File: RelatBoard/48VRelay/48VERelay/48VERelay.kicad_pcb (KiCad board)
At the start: 4 copper layers, 120 x 90 mm, 103 parts, among them J1 12, J10 Screw_Terminal_01x03, J11 Screw_Terminal_01x03, J12 Screw_Terminal_01x03, J13 Screw_Terminal_01x03, J14 Screw_Terminal_01x03, J2 RJ45_Hanrun_HR911105A_Horizon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, J4 TC2050, K10 G2RL-1-E, K11 G2RL-1-E, K12 G2RL-1-E, K13 G2RL-1-E, K14 G2RL-1-E, U1 ESP32-WROOM-32UE, U10 TLV1117LV33DCYR, U2 ULN2803A, U3 W5500, U4 3A 32V, U5 TPS630701RNMR, U7 TVS1800DRVR, U9 TLV1117LV33DCYR, Y2 ABM3C-25.000MHZ-D4Y-T

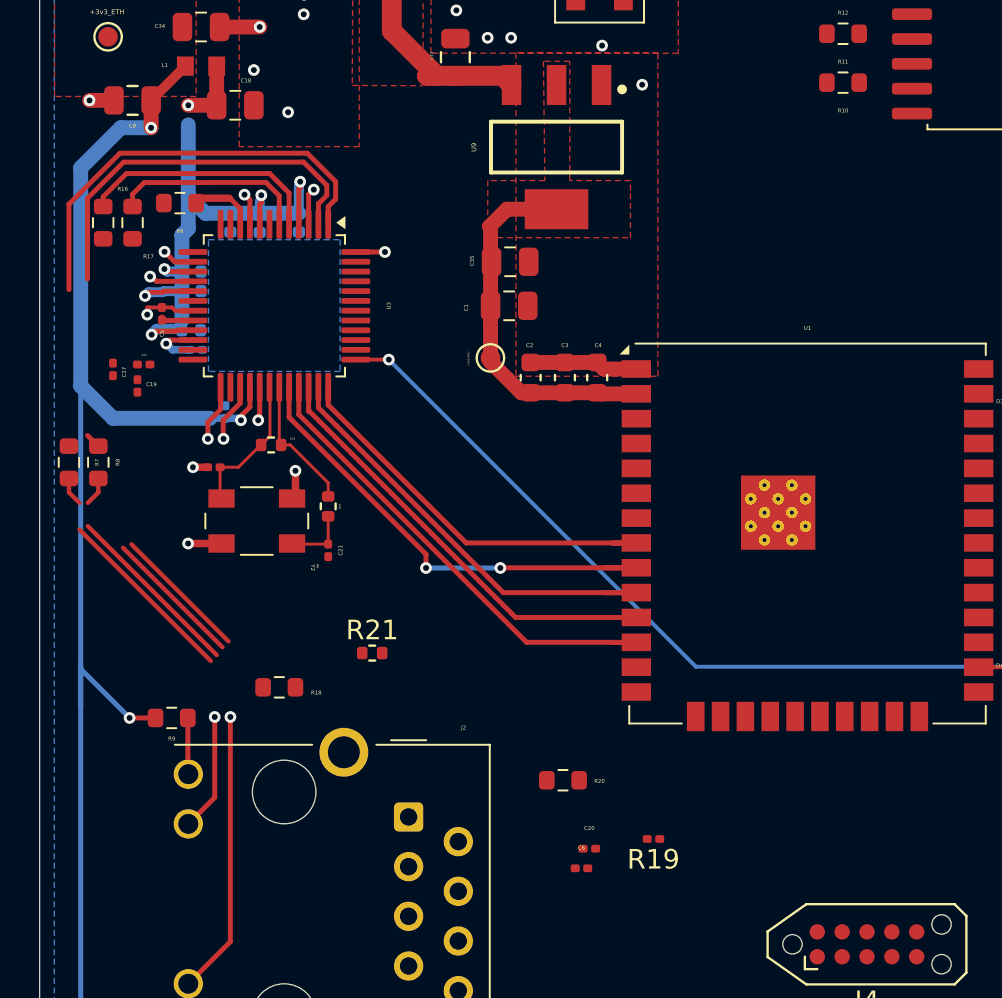
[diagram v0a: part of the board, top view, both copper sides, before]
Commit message: update tx/rx eth routing
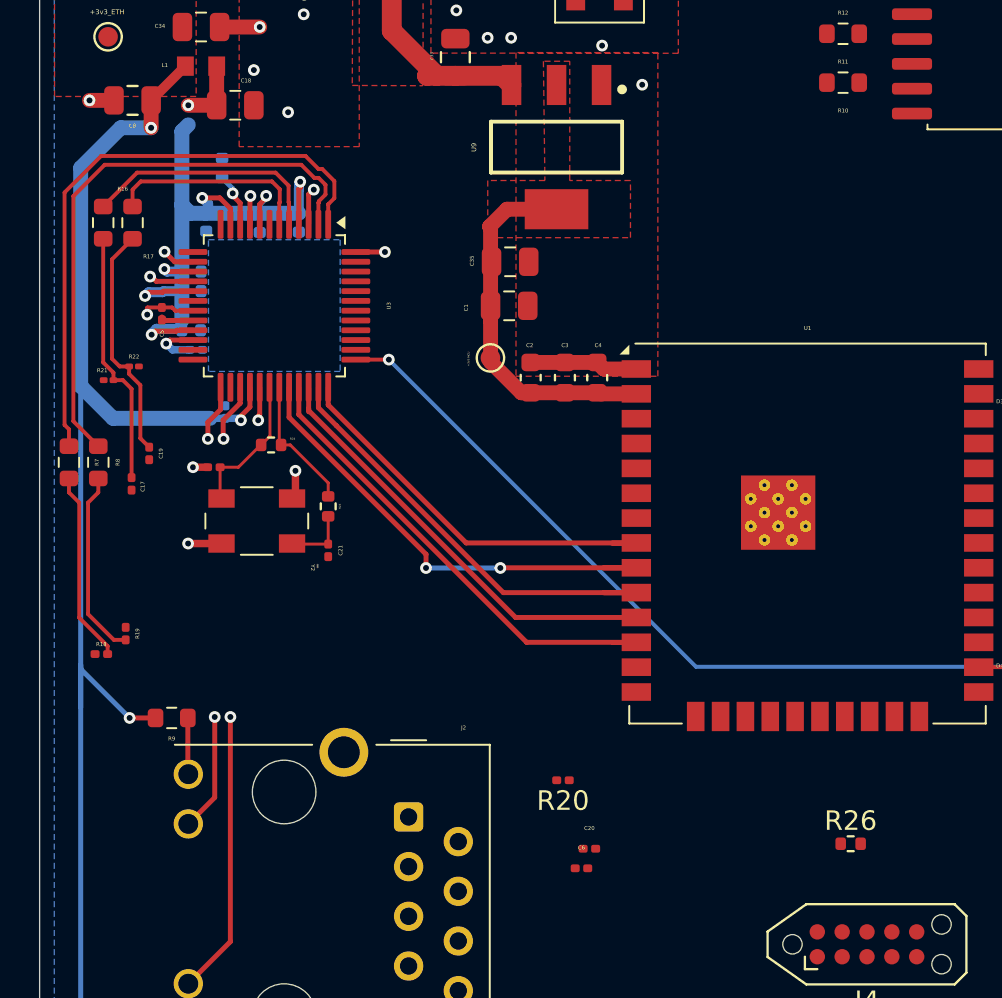
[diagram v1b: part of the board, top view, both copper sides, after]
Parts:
- added R26: 10kΩ, Resistor_SMD:R_0402_1005Metric, F.Cu at (81.5, 105.0)
- R18, R20: footprint Resistor_SMD:R_0603_1608Metric -> Resistor_SMD:R_0201_0603Metric
- R21: footprint Resistor_SMD:R_0402_1005Metric -> Resistor_SMD:R_01005_0402Metric
- R22: footprint Resistor_SMD:R_0201_0603Metric -> Resistor_SMD:R_01005_0402Metric
- R6: footprint Resistor_SMD:R_0603_1608Metric -> Resistor_SMD:R_0402_1005Metric; moved to B.Cu
- moved R19 28.9 mm to (44.4, 94.3), turned to -90 degrees
- moved R21 19.4 mm to (43.5, 81.3), turned to 180 degrees
- moved R18 9.25 mm to (43.2, 95.3), turned to 0 degrees
- moved C17 5.93 mm to (44.7, 86.6)
- moved C19 3.50 mm to (45.6, 85.0)
- moved R6 2.80 mm to (49.3, 70.5), turned to 90 degrees
- moved C13 1.24 mm to (48.5, 73.2)
- moved R22 0.50 mm to (44.8, 80.6)
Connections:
- net /MCU/TX_N renamed /MCU/PHY_RC_TXN
- net /MCU/TX_P renamed /MCU/PHY_RC_TXP
- net Net-(C17-Pad1) renamed /MCU/PHY_RC_RXN
- net Net-(C19-Pad1) renamed /MCU/PHY_RC_RXP
- net Net-(U3-RXN) renamed /MCU/PHY_R_RXN
- net Net-(U3-RXP) renamed /MCU/PHY_R_RXP
- net Net-(U3-TXN) renamed /MCU/PHY_R_TXN
- net Net-(U3-TXP) renamed /MCU/PHY_R_TXP
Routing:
- net /MCU/PHY_RC_RXN: track 0.00 -> 13.1 mm
- net /MCU/PHY_RC_RXP: track 0.00 -> 12.2 mm
- net /MCU/PHY_R_TXP: track 20.6 -> 29.5 mm
- net /MCU/PHY_R_TXN: track 22.0 -> 30.5 mm
- net /MCU/RX_N: track 7.19 -> 0.00 mm
- net /MCU/RX_P: track 7.01 -> 0.00 mm
- net +3V3A: track 38.5 -> 41.7 mm, vias 6 -> 7
- net /MCU/PHY_RC_TXN: track 11.0 -> 9.79 mm
- net /MCU/PHY_RC_TXP: track 10.8 -> 9.62 mm
- net Net-(U3-EXRES1): track 3.56 -> 2.75 mm, vias 0 -> 1

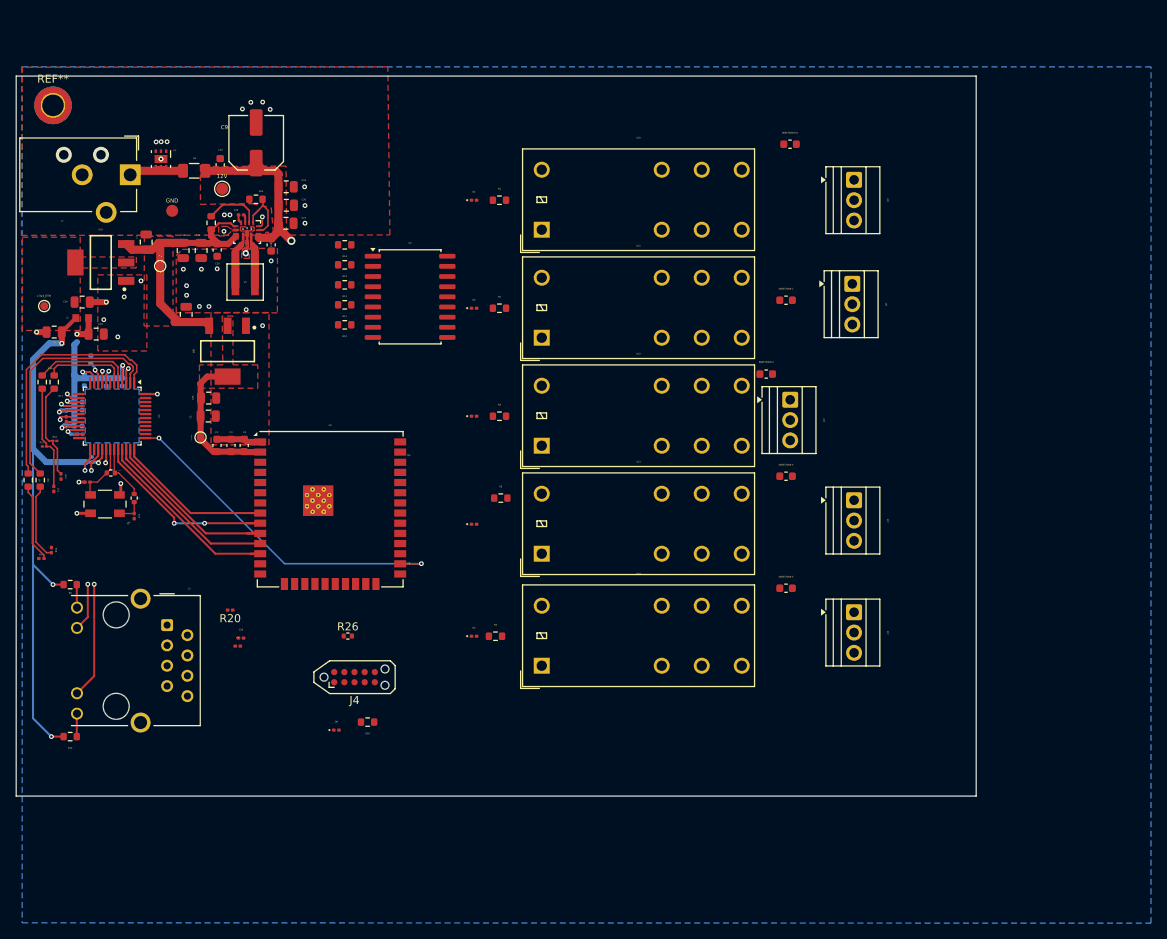
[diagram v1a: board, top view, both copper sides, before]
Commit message: JTAG left
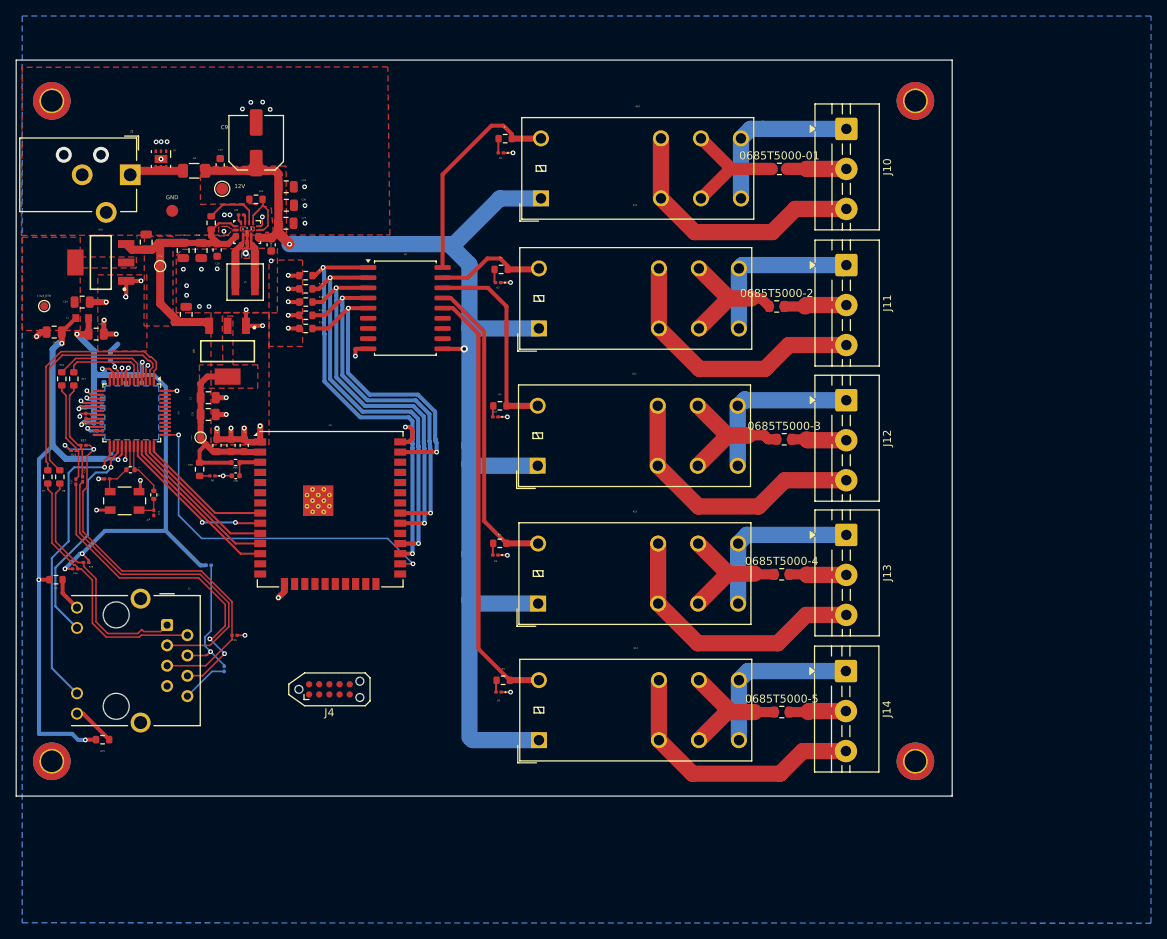
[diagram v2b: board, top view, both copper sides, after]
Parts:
- added C36: 1uF, Capacitor_SMD:C_0402_1005Metric, F.Cu at (67.4, 85.0)
- added REF**: MountingHole_2.7mm_M2.5_DIN965_Pad_TopBottom, MountingHole:MountingHole_2.7mm_M2.5_DIN965_Pad_TopBottom, F.Cu at (152.4, 120.7)
- added REF**: MountingHole_2.7mm_M2.5_DIN965_Pad_TopBottom, MountingHole:MountingHole_2.7mm_M2.5_DIN965_Pad_TopBottom, F.Cu at (152.4, 38.1)
- added REF**: MountingHole_2.7mm_M2.5_DIN965_Pad_TopBottom, MountingHole:MountingHole_2.7mm_M2.5_DIN965_Pad_TopBottom, F.Cu at (44.5, 120.7)
- 0685T5000-01, 0685T5000-2, 0685T5000-3, 0685T5000-4, 0685T5000-5: footprint Fuse:Fuse_0603_1608Metric -> Fuse:Fuse_0805_2012Metric
- C6, R20: moved to B.Cu
- J10, J11, J12, J13, J14: footprint TerminalBlock:TerminalBlock_Xinya_XY308-2.54-3P_1x03_P2.54mm_Horizontal -> TerminalBlock:TerminalBlock_MaiXu_MX126-5.0-03P_1x03_P5.00mm
- R13: value 10k -> 100k
- R21, R22: footprint Resistor_SMD:R_01005_0402Metric -> Resistor_SMD:R_0201_0603Metric
- moved R29 37.9 mm to (62.9, 84.2), turned to -90 degrees
- moved D6 35.3 mm to (64.5, 85.0), turned to 180 degrees
- moved R26 25.8 mm to (67.4, 83.3)
- moved 0685T5000-5 15.5 mm to (135.7, 114.5)
- moved 0685T5000-4 12.3 mm to (135.7, 97.3)
- moved K14 9.31 mm to (105.3, 118.0)
- moved 0685T5000-3 8.45 mm to (136.0, 80.4)
- moved R1 7.73 mm to (101.1, 42.8)
- moved D5 7.63 mm to (100.3, 112.0), turned to 180 degrees
- moved J14 7.43 mm to (143.7, 109.4)
- moved J12 7.01 mm to (143.8, 75.5)
- moved D1 6.80 mm to (100.6, 44.6), turned to 180 degrees
- moved J10 6.44 mm to (143.8, 41.6)
- moved K13 6.25 mm to (105.2, 100.9)
- moved R20 6.21 mm to (64.1, 96.2), turned to 0 degrees
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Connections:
- net /MCU/JTAG_RESET renamed JTAG_RESET
- C17 pad 2: /MCU/RX_N -> RX_N
- C19 pad 2: /MCU/RX_P -> RX_P
- C20 pad 2: /MCU/RX_CT -> RX_CT
- C6 pad 1: /MCU/TX_CT -> TX_CT
- J2 pad 1: unconnected-(J2-TD+-Pad1) -> TX_P
- J2 pad 10: /Connectors/ACT_LED -> ACT_LED
- J2 pad 11: /Connectors/LINK_LED -> LINK_LED
- J2 pad 2: /Connectors/RX_CT -> TX_N
- J2 pad 3: /Connectors/RX_P -> RX_P
- J2 pad 4: /Connectors/RX_N -> TX_CT
- J2 pad 5: /Connectors/TX_N -> RX_CT
- J2 pad 6: /Connectors/TX_CT -> RX_N
- R10 pad 1: /Outputs/MCU_RELAY_5 -> MCU_RELAY_5
- R11 pad 1: /Outputs/MCU_RELAY_4 -> MCU_RELAY_4
- R12 pad 1: /Outputs/MCU_RELAY_3 -> MCU_RELAY_3
- R13 pad 1: /Outputs/MCU_RELAY_2 -> MCU_RELAY_2
- R14 pad 1: /Outputs/MCU_RELAY_1 -> MCU_RELAY_1
- R18 pad 2: /MCU/PHY_RC_TXN -> TX_N
- R19 pad 2: /MCU/PHY_RC_TXP -> TX_P
- R20 pad 2: /MCU/TX_CT -> TX_CT
- R21 pad 2: /MCU/RX_CT -> RX_CT
- R22 pad 2: /MCU/RX_CT -> RX_CT
- R7 pad 2: /MCU/PHY_RC_TXN -> TX_N
- R8 pad 2: /MCU/PHY_RC_TXP -> TX_P
- U1 pad 25: unconnected-(U1-IO0-Pad25) -> UART_EN
- U1 pad 27: /MCU/MCU_RELAY_1 -> MCU_RELAY_1
- U1 pad 28: /MCU/MCU_RELAY_2 -> MCU_RELAY_2
- U1 pad 30: /MCU/MCU_RELAY_3 -> MCU_RELAY_3
- U1 pad 31: /MCU/MCU_RELAY_4 -> MCU_RELAY_4
- U1 pad 34: unconnected-(U1-RXD0/IO3-Pad34) -> UART_RXD
- U1 pad 35: unconnected-(U1-TXD0/IO1-Pad35) -> UART_TXD
- U1 pad 37: /MCU/MCU_RELAY_5 -> MCU_RELAY_5
- U2 pad 1: /Outputs/MCU_RELAY_1 -> MCU_RELAY_1
- U2 pad 2: /Outputs/MCU_RELAY_2 -> MCU_RELAY_2
- U2 pad 3: /Outputs/MCU_RELAY_3 -> MCU_RELAY_3
- U2 pad 4: /Outputs/MCU_RELAY_4 -> MCU_RELAY_4
- U2 pad 5: /Outputs/MCU_RELAY_5 -> MCU_RELAY_5
- U3 pad 25: /MCU/LINK_LED -> LINK_LED
- U3 pad 27: /MCU/ACT_LED -> ACT_LED
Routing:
- net +12V: track 26.8 -> 169.5 mm, vias 1 -> 2
- net /Outputs/Relay_5: track 0.00 -> 54.2 mm
- net RX_CT: track 0.00 -> 53.4 mm, vias 0 -> 2
- net MCU_RELAY_1: track 0.00 -> 52.9 mm, vias 0 -> 2
- net GND: track 31.4 -> 83.0 mm, vias 47 -> 69
- net MCU_RELAY_2: track 0.00 -> 51.2 mm, vias 0 -> 2
- net MCU_RELAY_3: track 0.00 -> 48.3 mm, vias 0 -> 2
- net +3V3A: track 41.7 -> 88.4 mm, vias 7 -> 9
- net MCU_RELAY_4: track 0.00 -> 46.7 mm, vias 0 -> 2
- net RX_N: track 0.00 -> 42.2 mm, vias 0 -> 2
- net RX_P: track 0.00 -> 40.5 mm
- net MCU_RELAY_5: track 0.00 -> 38.7 mm, vias 0 -> 2
- net /Outputs/Relay_4: track 0.00 -> 38.6 mm
- net LINK_LED: track 0.00 -> 37.4 mm, vias 0 -> 1
- net /Outputs/NC_4: track 0.00 -> 34.5 mm
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- added copper zone on In1.Cu, net GND
- added copper zone on In2.Cu, net GND
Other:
- board size 120 x 90 mm -> 117 x 92 mm

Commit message: update relay traces
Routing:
- net GND: track 83.0 -> 87.7 mm, vias 69 -> 72
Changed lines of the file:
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@@
 	)
 	(segment
+		(start 64.237493 45.314493)
+		(end 64.008 45.085)
+		(width 0.2)
+		(layer "F.Cu")
+		(net "GND")
+	)
+	(segment
 		(start 49.386934 77.35)
 		(end 49.221934 77.185)
@@
 	)
 	(segment
+		(start 56.25 53.224)
+		(end 56.261 53.213)
+		(width 0.2)
+		(layer "F.Cu")
+		(net "GND")
+	)
+	(segment
 		(start 70.787 66.213)
 		(end 70.8 66.2)
@@
 	)
 	(segment
+		(start 65.5 43.847)
+		(end 65.532 43.815)
+		(width 0.2)
+		(layer "F.Cu")
+		(net "GND")
+	)
+	(segment
 		(start 73.535 99.439)
 		(end 72.771 100.203)
@@
 	)
 	(segment
+		(start 65.5 45.314493)
+		(end 65.5 43.847)
+		(width 0.2)
+		(layer "F.Cu")
+		(net "GND")
+	)
+	(segment
 		(start 50.95 67.25)
 		(end 50.95 65.55)
@@
 	)
 	(segment
+		(start 56.25 54.8)
+		(end 56.25 53.224)
+		(width 1.016)
+		(layer "F.Cu")
+		(net "GND")
+	)
+	(segment
 		(start 50.95 65.55)
 		(end 51 65.5)
@@
 	)
 	(segment
+		(start 65.5 45.314493)
+		(end 64.237493 45.314493)
+		(width 0.2)
+		(layer "F.Cu")
+		(net "GND")
+	)
+	(segment
 		(start 68.120002 53.349493)
 		(end 67.8 53.029491)
@@
 	)
 	(via
+		(at 65.532 43.815)
+		(size 0.6)
+		(drill 0.3)
+		(layers "F.Cu" "B.Cu")
+		(net "GND")
+	)
+	(via
 		(at 65.1 79.05)
 		(size 0.6)
@@
 	)
 	(via
+		(at 64.008 45.085)
+		(size 0.6)
+		(drill 0.3)
+		(layers "F.Cu" "B.Cu")
+		(net "GND")
+	)
+	(via
 		(at 82.4 70)
 		(size 0.6)
@@
 	)
 	(via
+		(at 56.261 53.213)
+		(size 0.6)
+		(drill 0.3)
+		(layers "F.Cu" "B.Cu")
+		(net "GND")
+	)
+	(via
 		(at 53.226305 71.4858)
 		(size 0.6)
@@
 	)
 	(segment
-		(start 89.6 95.97)
-		(end 86.43 92.8)
+		(start 89.558 96.012)
+		(end 83.566 96.012)
+		(width 0.2)
+		(layer "B.Cu")
+		(net "/MCU/Ether_RESET")
+	)
+	(segment
+		(start 60.3 89.9)
+		(end 60.3 79.85)
+		(width 0.2)
+		(layer "B.Cu")
+		(net "/MCU/Ether_RESET")
+	)
+	(segment
+		(start 83.566 96.012)
+		(end 80.354 92.8)
 		(width 0.2)
 		(layer "B.Cu")
@@
 	)
 	(segment
-		(start 60.3 89.9)
-		(end 60.3 79.85)
+		(start 80.354 92.8)
+		(end 63.2 92.8)
 		(width 0.2)
 		(layer "B.Cu")
@@
 	)
 	(segment
-		(start 86.43 92.8)
-		(end 63.2 92.8)
+		(start 89.6 95.97)
+		(end 89.558 96.012)
 		(width 0.2)
 		(layer "B.Cu")

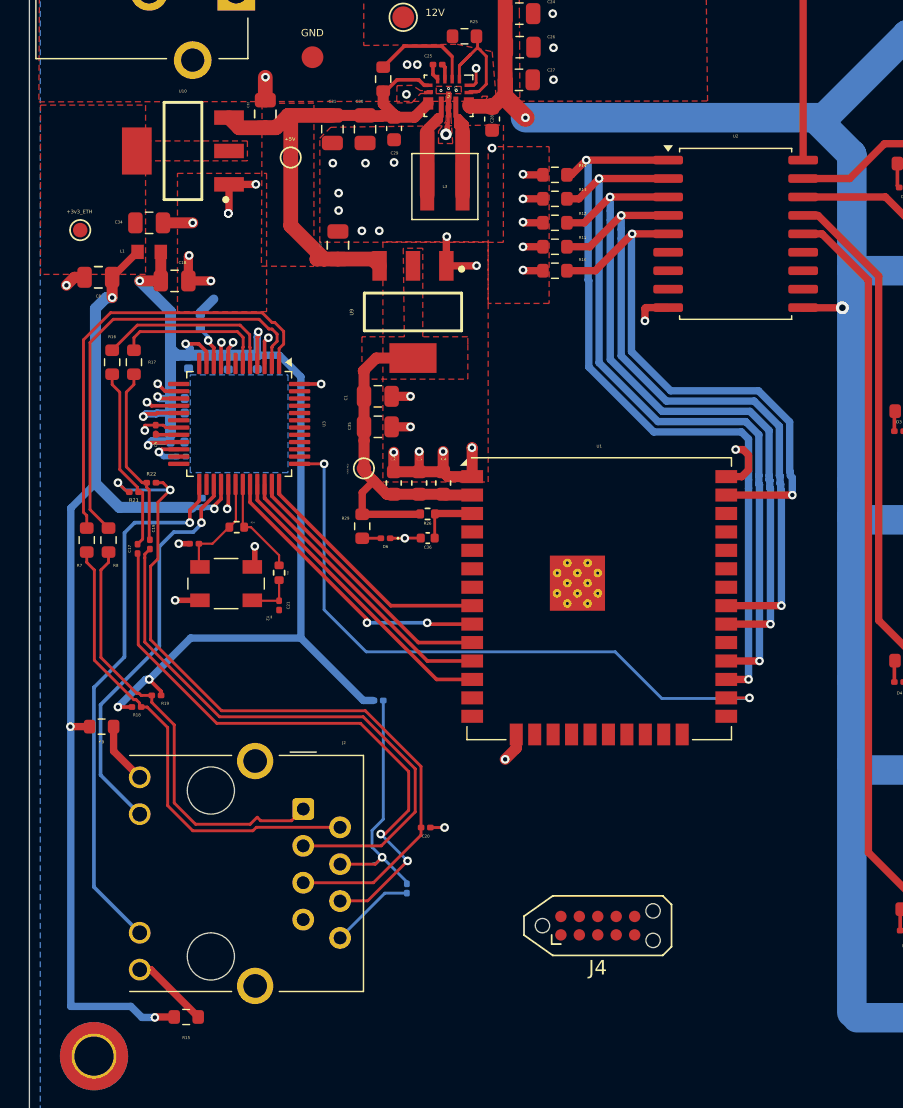
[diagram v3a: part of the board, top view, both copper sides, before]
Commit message: update schematic footprint and rule set
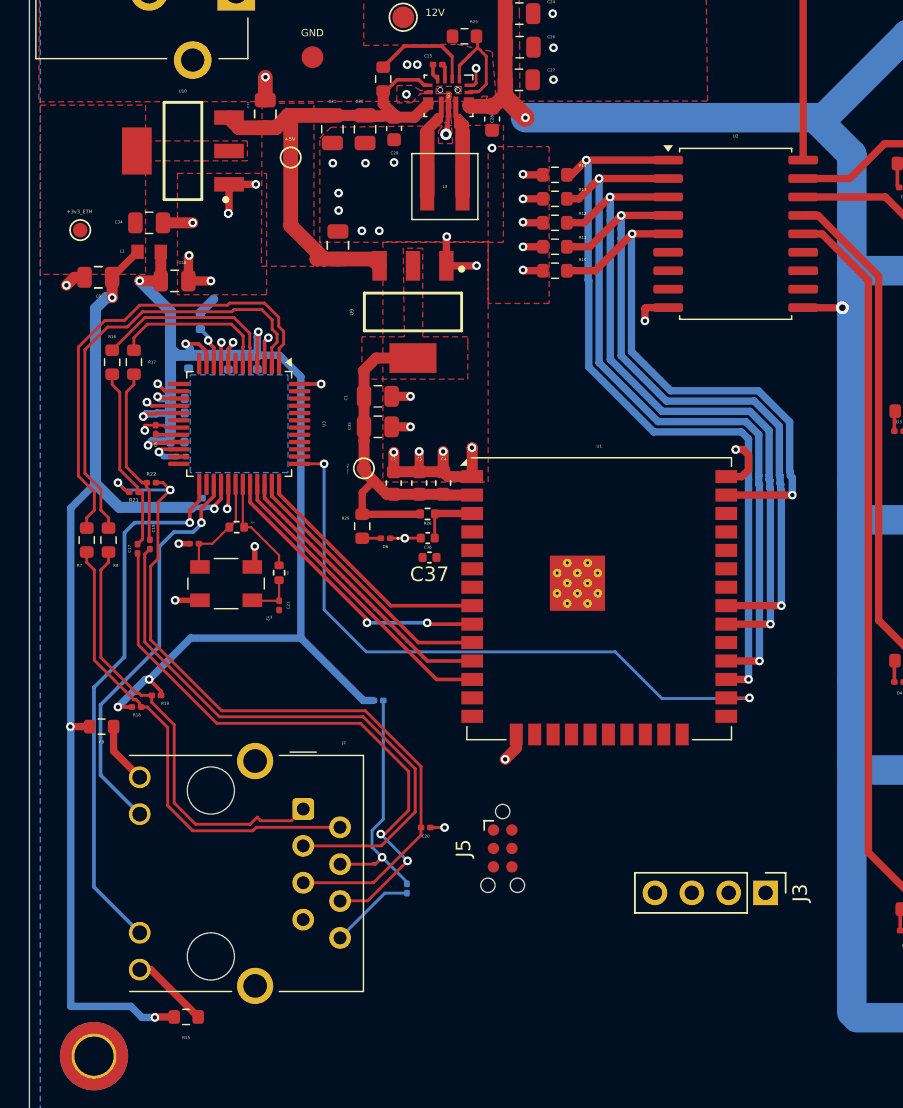
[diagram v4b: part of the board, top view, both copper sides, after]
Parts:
- removed J4: TC2050, Connector:Tag-Connect_TC2050-IDC-NL_2x05_P1.27mm_Vertical
- added C37: 1uF, Capacitor_SMD:C_0402_1005Metric, F.Cu at (67.6, 86.3)
- added J3: B4B-PH-SM4-TB, Connector_PinHeader_2.54mm:PinHeader_1x04_P2.54mm_Vertical, F.Cu at (90.7, 109.4)
- added J5: TC2030, Connector:Tag-Connect_TC2030-IDC-NL_2x03_P1.27mm_Vertical, F.Cu at (72.6, 106.3)
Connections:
- net +3V3 MCU renamed JTAG_VREF
- net JTAG_RESET renamed Net-(U1-EN)
- net UART_EN renamed Net-(U1-IO0)
- U1 pad 13: /MCU/JTAG_TMS -> JTAG_TMS
- U1 pad 14: /MCU/JTAG_TDI -> JTAG_TDI
- U1 pad 16: /MCU/JTAG_TCK -> JTAG_TCK
- U1 pad 23: /MCU/JTAG_TDO -> JTAG_TDO
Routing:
- net /MCU/PHY_R_TXN: track 30.5 -> 32.1 mm
- net /MCU/PHY_R_TXP: track 29.5 -> 30.6 mm
- net GND: vias 72 -> 71
- added copper zone on F.Cu, net (none)
- removed copper zone on F.Cu, net JTAG_VREF
